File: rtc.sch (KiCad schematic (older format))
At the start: 20 parts, among them IC10 74LS125, IC3 74LS245, IC5 MM58167B, IC6 74LS32, IC83 74LS32, IC88 74LS08, IC9 74LS138

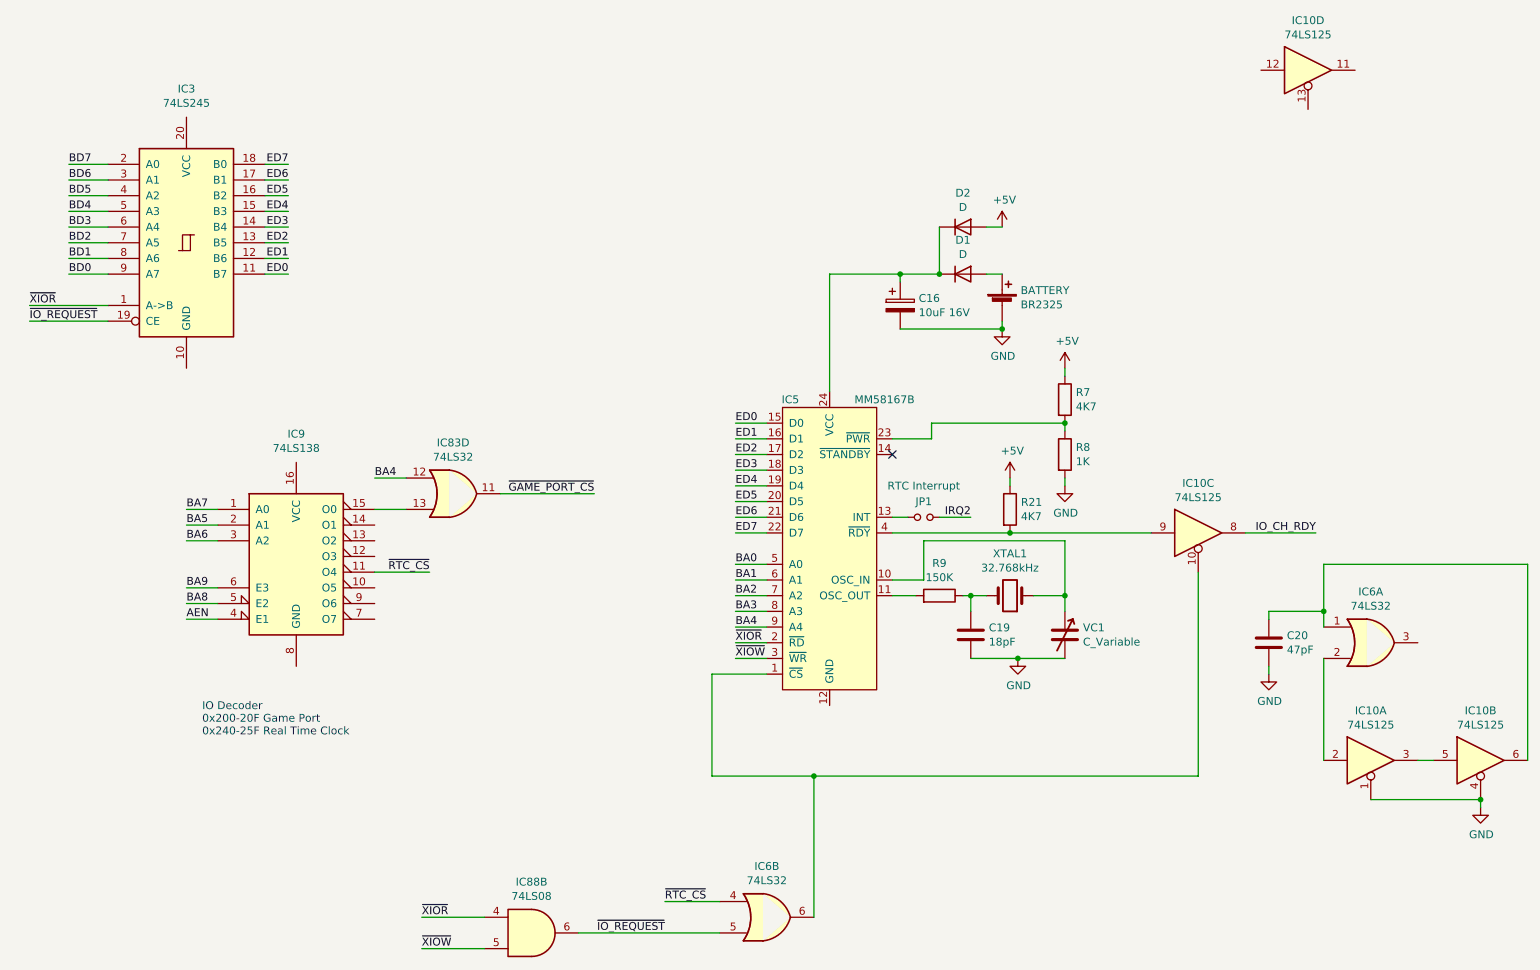
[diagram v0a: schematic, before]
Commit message: Tidy up and map all signals
This fixes up the schematic to:
 - Look presentable
 - Fix all labels connecting sheets
 - Tidy up all loose ends by either inspecting the PCB under
    magnification, measuring with an oscillosope or buzzing
    out with a meter
 - Pass ERC (with 1 exception due to incorrect circuitry around
    pin 33 on the FPU (~RQ~/~GT1~)
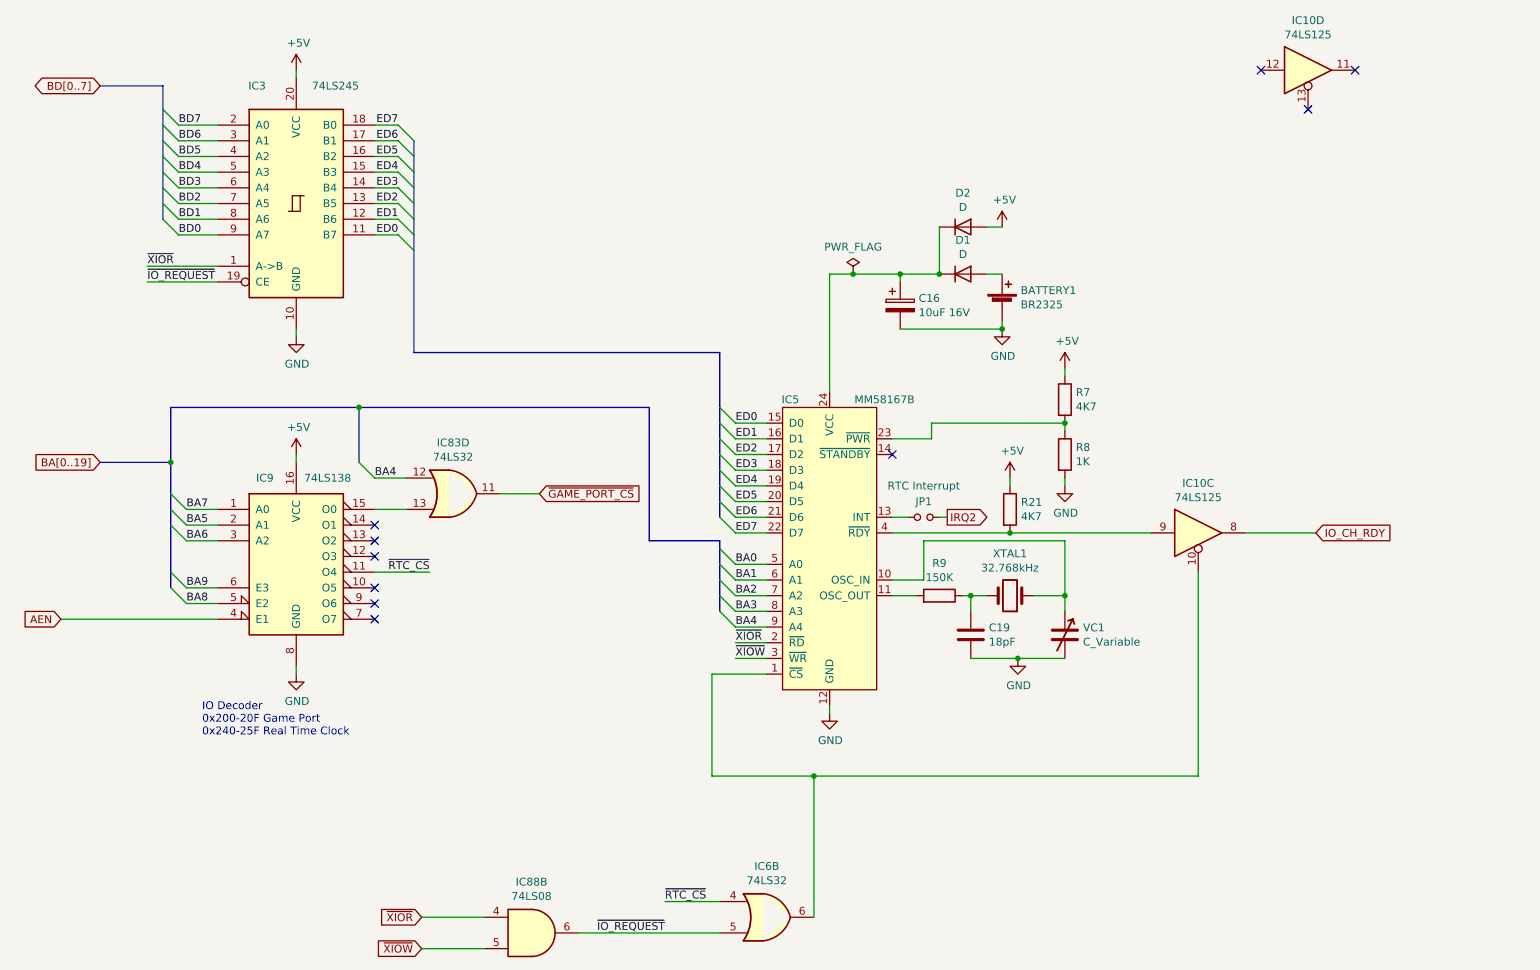
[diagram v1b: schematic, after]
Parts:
- removed C20: 47pF, symbol Device:C
- removed unit 1 of IC10
- removed unit 2 of IC10
- removed unit 1 of IC6
- renumbered BATTERY to BATTERY1
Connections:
- net +5V: now also IC3.20 (VCC), IC9.16 (VCC)
- net GND: now also IC3.10 (GND), IC5.12 (GND), IC9.8 (GND)
- no-connect marks 1 -> 10
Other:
- moved on the sheet: IC3
